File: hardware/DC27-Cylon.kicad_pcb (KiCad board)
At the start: 2 copper layers, 79 x 102 mm, 78 parts, among them J1 CONN_04LOCK, J2 CONN_05LOCK, U1 STM32F030K6Tx, U2 AZ1117-3.3, U3 74HC595D_118, U4 74HC595D_118, U5 74HC595D_118, Y1 16MHz

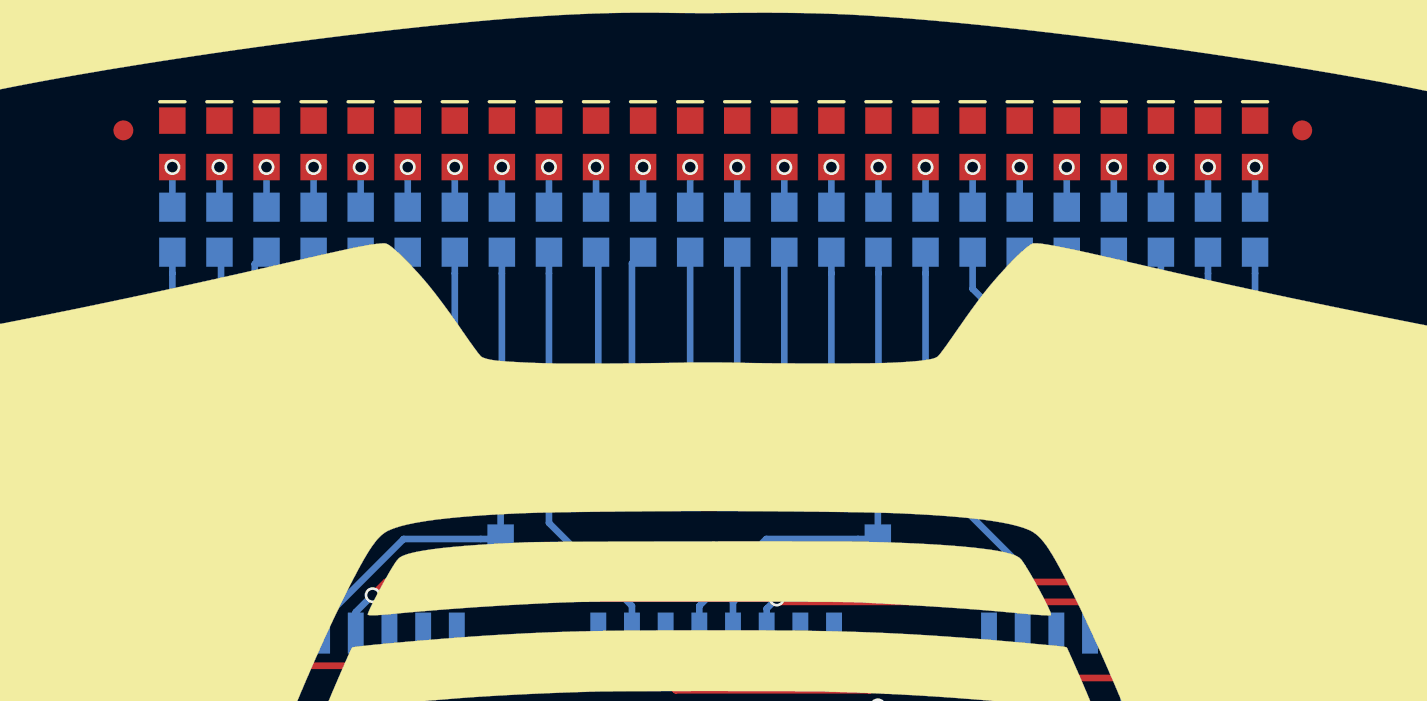
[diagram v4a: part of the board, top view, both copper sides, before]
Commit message: Remove via in pad
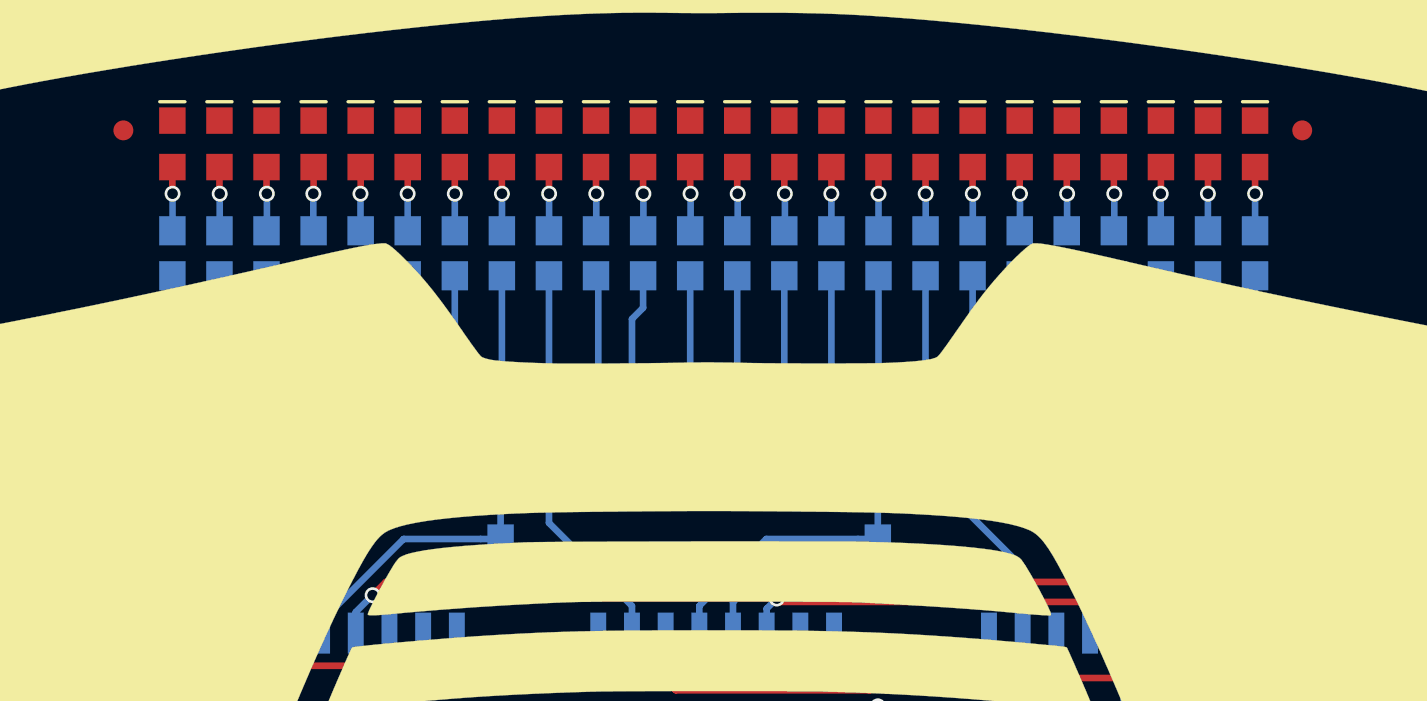
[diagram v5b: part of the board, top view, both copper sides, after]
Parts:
- removed the G*** at (59.4, 73.4) (x2)
- added G*** (x2): LOGO, LOGO, F.Cu at (59.4, 73.4)
- moved R1 0.89 mm to (80.0, 80.3)
- moved R10 0.89 mm to (64.0, 80.3)
- moved R11 0.89 mm to (62.3, 80.3)
- moved R12 0.89 mm to (60.5, 80.3)
- moved R13 0.89 mm to (58.7, 80.3)
- moved R14 0.89 mm to (56.9, 80.3)
- moved R15 0.89 mm to (55.2, 80.3)
- moved R16 0.89 mm to (53.4, 80.3)
- moved R17 0.89 mm to (51.6, 80.3)
- moved R18 0.89 mm to (49.8, 80.3)
- moved R19 0.89 mm to (48.1, 80.3)
- moved R2 0.89 mm to (78.2, 80.3)
- moved R20 0.89 mm to (46.3, 80.3)
- moved R21 0.89 mm to (44.5, 80.3)
- moved R22 0.89 mm to (42.7, 80.3)
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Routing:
- net Net-(D11-PadA): track 1.51 -> 2.42 mm
- net Net-(D12-PadA): track 1.51 -> 2.42 mm
- net Net-(D4-PadA): track 1.51 -> 2.42 mm
- net Net-(D13-PadA): track 1.51 -> 2.41 mm
- net Net-(D5-PadA): track 1.51 -> 2.41 mm
- net Net-(D22-PadA): track 1.51 -> 2.41 mm
- net Net-(D14-PadA): track 1.51 -> 2.41 mm
- net Net-(D6-PadA): track 1.51 -> 2.41 mm
- net Net-(D23-PadA): track 1.51 -> 2.41 mm
- net Net-(D21-PadA): track 1.51 -> 2.41 mm
- net Net-(D15-PadA): track 1.51 -> 2.41 mm
- net Net-(D7-PadA): track 1.51 -> 2.41 mm
- net Net-(D24-PadA): track 1.51 -> 2.41 mm
- net Net-(D20-PadA): track 1.51 -> 2.41 mm
- net Net-(D3-PadA): track 1.51 -> 2.41 mm
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
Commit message: Add SAO to head
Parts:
- removed the G*** at (59.4, 73.4) (x2)
- added G*** (x2): LOGO, LOGO, F.Cu at (59.4, 73.4)
- added SAO1: SAO, Sparkfun_Connectors:2X3, F.Cu at (41.5, 54.3)
- renumbered D24 to D1, D15 to D1, D14 to D1, D13 to D1, D12 to D1, D11 to D1, D10 to D1, D9 to D1, D8 to D1, D7 to D1, D6 to D1, D23 to D1, D5 to D1, D4 to D1, D3 to D1, D2 to D1, D22 to D1, D21 to D1, D20 to D1, D19 to D1, D18 to D1, D17 to D1, D16 to D1, R24 to R1, R15 to R1, R14 to R1, R13 to R1, R12 to R1, R11 to R1, R10 to R1, R9 to R1, R8 to R1, R7 to R1, R6 to R1, R23 to R1, R5 to R1, R4 to R1, R3 to R1, R2 to R1, R22 to R1, R21 to R1, R20 to R1, R19 to R1, R18 to R1, R17 to R1, R16 to R1
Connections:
- D1 pad A: Net-(D24-PadA) -> Net-(D1-PadA)
- D1 pad A: Net-(D15-PadA) -> Net-(D1-PadA)
- D1 pad A: Net-(D14-PadA) -> Net-(D1-PadA)
- D1 pad A: Net-(D13-PadA) -> Net-(D1-PadA)
- D1 pad A: Net-(D12-PadA) -> Net-(D1-PadA)
- D1 pad A: Net-(D11-PadA) -> Net-(D1-PadA)
- D1 pad A: Net-(D10-PadA) -> Net-(D1-PadA)
- D1 pad A: Net-(D9-PadA) -> Net-(D1-PadA)
- D1 pad A: Net-(D8-PadA) -> Net-(D1-PadA)
- D1 pad A: Net-(D7-PadA) -> Net-(D1-PadA)
- D1 pad A: Net-(D6-PadA) -> Net-(D1-PadA)
- D1 pad A: Net-(D23-PadA) -> Net-(D1-PadA)
- D1 pad A: Net-(D5-PadA) -> Net-(D1-PadA)
- D1 pad A: Net-(D4-PadA) -> Net-(D1-PadA)
- D1 pad A: Net-(D3-PadA) -> Net-(D1-PadA)
- D1 pad A: Net-(D2-PadA) -> Net-(D1-PadA)
- D1 pad A: Net-(D22-PadA) -> Net-(D1-PadA)
- D1 pad A: Net-(D21-PadA) -> Net-(D1-PadA)
- D1 pad A: Net-(D20-PadA) -> Net-(D1-PadA)
- D1 pad A: Net-(D19-PadA) -> Net-(D1-PadA)
- D1 pad A: Net-(D18-PadA) -> Net-(D1-PadA)
- D1 pad A: Net-(D17-PadA) -> Net-(D1-PadA)
- D1 pad A: Net-(D16-PadA) -> Net-(D1-PadA)
- R1 pad 1: /LED23 -> /LED0
- R1 pad 2: Net-(D24-PadA) -> Net-(D1-PadA)
- R1 pad 1: /LED14 -> /LED0
- R1 pad 2: Net-(D15-PadA) -> Net-(D1-PadA)
- R1 pad 1: /LED13 -> /LED0
- R1 pad 2: Net-(D14-PadA) -> Net-(D1-PadA)
- R1 pad 1: /LED12 -> /LED0
- R1 pad 2: Net-(D13-PadA) -> Net-(D1-PadA)
- R1 pad 1: /LED11 -> /LED0
- R1 pad 2: Net-(D12-PadA) -> Net-(D1-PadA)
- R1 pad 1: /LED10 -> /LED0
- R1 pad 2: Net-(D11-PadA) -> Net-(D1-PadA)
- R1 pad 1: /LED9 -> /LED0
- R1 pad 2: Net-(D10-PadA) -> Net-(D1-PadA)
- R1 pad 1: /LED8 -> /LED0
- R1 pad 2: Net-(D9-PadA) -> Net-(D1-PadA)
- R1 pad 1: /LED7 -> /LED0
- R1 pad 2: Net-(D8-PadA) -> Net-(D1-PadA)
- R1 pad 1: /LED6 -> /LED0
- R1 pad 2: Net-(D7-PadA) -> Net-(D1-PadA)
- R1 pad 1: /LED5 -> /LED0
- R1 pad 2: Net-(D6-PadA) -> Net-(D1-PadA)
- R1 pad 1: /LED22 -> /LED0
- R1 pad 2: Net-(D23-PadA) -> Net-(D1-PadA)
- R1 pad 1: /LED4 -> /LED0
- R1 pad 2: Net-(D5-PadA) -> Net-(D1-PadA)
- R1 pad 1: /LED3 -> /LED0
- R1 pad 2: Net-(D4-PadA) -> Net-(D1-PadA)
- R1 pad 1: /LED2 -> /LED0
- R1 pad 2: Net-(D3-PadA) -> Net-(D1-PadA)
- R1 pad 1: /LED1 -> /LED0
- R1 pad 2: Net-(D2-PadA) -> Net-(D1-PadA)
- R1 pad 1: /LED21 -> /LED0
- R1 pad 2: Net-(D22-PadA) -> Net-(D1-PadA)
- R1 pad 1: /LED20 -> /LED0
- R1 pad 2: Net-(D21-PadA) -> Net-(D1-PadA)
- R1 pad 1: /LED19 -> /LED0
- R1 pad 2: Net-(D20-PadA) -> Net-(D1-PadA)
- R1 pad 1: /LED18 -> /LED0
- R1 pad 2: Net-(D19-PadA) -> Net-(D1-PadA)
- R1 pad 1: /LED17 -> /LED0
- R1 pad 2: Net-(D18-PadA) -> Net-(D1-PadA)
- R1 pad 1: /LED16 -> /LED0
- R1 pad 2: Net-(D17-PadA) -> Net-(D1-PadA)
- R1 pad 1: /LED15 -> /LED0
- R1 pad 2: Net-(D16-PadA) -> Net-(D1-PadA)
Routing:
- net Net-(D1-PadA): track 2.40 -> 57.8 mm, vias 1 -> 24
- net Net-(D11-PadA): track 2.42 -> 0.00 mm, vias 1 -> 0
- net Net-(D12-PadA): track 2.42 -> 0.00 mm, vias 1 -> 0
- net Net-(D4-PadA): track 2.42 -> 0.00 mm, vias 1 -> 0
- net Net-(D13-PadA): track 2.41 -> 0.00 mm, vias 1 -> 0
- net Net-(D5-PadA): track 2.41 -> 0.00 mm, vias 1 -> 0
- net Net-(D22-PadA): track 2.41 -> 0.00 mm, vias 1 -> 0
- net Net-(D14-PadA): track 2.41 -> 0.00 mm, vias 1 -> 0
- net Net-(D6-PadA): track 2.41 -> 0.00 mm, vias 1 -> 0
- net Net-(D23-PadA): track 2.41 -> 0.00 mm, vias 1 -> 0
- net Net-(D21-PadA): track 2.41 -> 0.00 mm, vias 1 -> 0
- net Net-(D15-PadA): track 2.41 -> 0.00 mm, vias 1 -> 0
- net Net-(D7-PadA): track 2.41 -> 0.00 mm, vias 1 -> 0
- net Net-(D24-PadA): track 2.41 -> 0.00 mm, vias 1 -> 0
- net Net-(D20-PadA): track 2.41 -> 0.00 mm, vias 1 -> 0
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
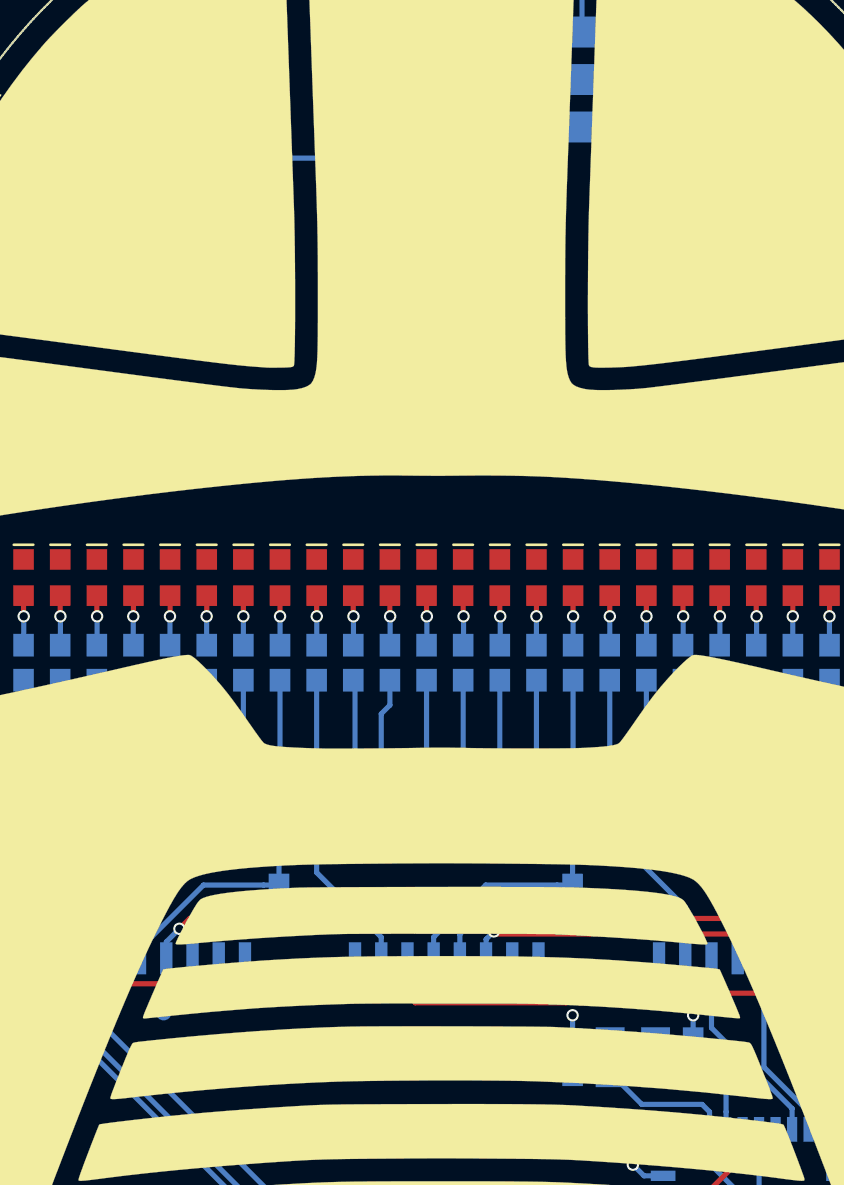
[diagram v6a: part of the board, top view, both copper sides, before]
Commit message: Move some small traces a little, update BOMs
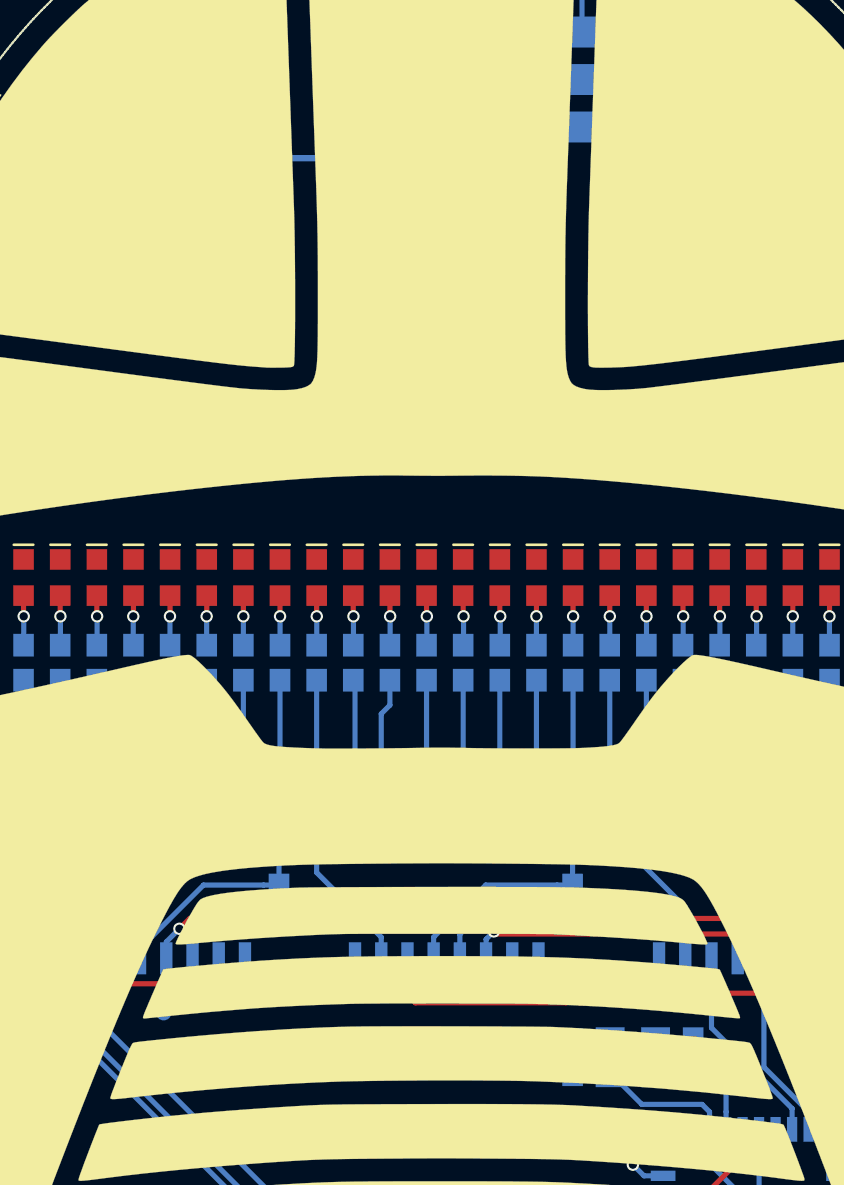
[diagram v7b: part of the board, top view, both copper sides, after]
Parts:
- removed the G*** at (59.4, 73.4) (x2)
- added G*** (x2): LOGO, LOGO, F.Cu at (59.4, 73.4)
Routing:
- net GND: track 54.1 -> 61.6 mm
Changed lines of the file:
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@@
     (thickness 1.6)
     (drawings 1827)
-    (tracks 411)
+    (tracks 414)
     (zones 0)
     (modules 79)
@@
   (page A4)
   (layers
-    (0 F.Cu signal)
+    (0 F.Cu signal hide)
     (31 B.Cu signal)
-    (32 B.Adhes user)
-    (33 F.Adhes user)
-    (34 B.Paste user)
-    (35 F.Paste user)
-    (36 B.SilkS user)
-    (37 F.SilkS user)
-    (38 B.Mask user)
-    (39 F.Mask user)
+    (32 B.Adhes user hide)
+    (33 F.Adhes user hide)
+    (34 B.Paste user hide)
+    (35 F.Paste user hide)
+    (36 B.SilkS user hide)
+    (37 F.SilkS user hide)
+    (38 B.Mask user hide)
+    (39 F.Mask user hide)
     (40 Dwgs.User user)
     (41 Cmts.User user)
@@
   (gr_line (start 59.86389 116.45791) (end 60.078076 116.45391) (layer Edge.Cuts) (width 0.1))
   (gr_line (start 60.078076 116.45391) (end 60.078842 116.44949) (layer Edge.Cuts) (width 0.1))
-  (segment (start 65.994 54.37) (end 64.484 55.88) (width 0.25) (layer B.Cu) (net 1))
+  (segment (start 65.994 54.37) (end 64.484 55.88) (width 0.3048) (layer B.Cu) (net 1))
   (segment (start 66.244 54.37) (end 65.994 54.37) (width 0.25) (layer B.Cu) (net 1))
-  (segment (start 45.446 58.801) (end 44.196 58.801) (width 0.25) (layer B.Cu) (net 1))
-  (segment (start 48.367 55.88) (end 45.446 58.801) (width 0.25) (layer B.Cu) (net 1))
-  (segment (start 64.484 55.88) (end 48.367 55.88) (width 0.25) (layer B.Cu) (net 1))
+  (segment (start 45.446 58.801) (end 44.196 58.801) (width 0.3048) (layer B.Cu) (net 1))
+  (segment (start 48.367 55.88) (end 45.446 58.801) (width 0.3048) (layer B.Cu) (net 1))
+  (segment (start 64.484 55.88) (end 48.367 55.88) (width 0.3048) (layer B.Cu) (net 1))
   (segment (start 68.98764 54.37) (end 69.00164 54.356) (width 0.25) (layer B.Cu) (net 1))
   (segment (start 66.244 54.37) (end 68.98764 54.37) (width 0.25) (layer B.Cu) (net 1))
@@
   (segment (start 59.055 94.648) (end 59.055 93.623) (width 0.25) (layer B.Cu) (net 2))
   (segment (start 61.57836 91.09964) (end 65.03689 91.09964) (width 0.25) (layer B.Cu) (net 2))
-  (via (at 71.628 97.409) (size 0.6) (drill 0.4) (layers F.Cu B.Cu) (net 2))
-  (segment (start 71.628 98.54164) (end 71.628 97.409) (width 0.25) (layer B.Cu) (net 2))
-  (via (at 65.786 97.409) (size 0.6) (drill 0.4) (layers F.Cu B.Cu) (net 2))
-  (segment (start 65.786 98.59264) (end 65.786 97.409) (width 0.25) (layer B.Cu) (net 2))
   (via (at 68.707 104.648) (size 0.6) (drill 0.4) (layers F.Cu B.Cu) (net 2))
   (segment (start 70.172 104.388) (end 68.967 104.388) (width 0.25) (layer B.Cu) (net 2))
@@
   (segment (start 69.247 105.188) (end 68.707 104.648) (width 0.25) (layer B.Cu) (net 2))
   (segment (start 70.172 105.188) (end 69.247 105.188) (width 0.25) (layer B.Cu) (net 2))
+  (via (at 64.516 98.552) (size 0.6) (drill 0.4) (layers F.Cu B.Cu) (net 2))
+  (segment (start 65.786 98.59264) (end 64.55664 98.59264) (width 0.25) (layer B.Cu) (net 2))
+  (segment (start 64.55664 98.59264) (end 64.516 98.552) (width 0.25) (layer B.Cu) (net 2))
+  (segment (start 64.516 98.552) (end 71.755 98.552) (width 0.25) (layer F.Cu) (net 2))
+  (via (at 72.644 99.314) (size 0.6) (drill 0.4) (layers F.Cu B.Cu) (net 2))
+  (segment (start 71.628 98.54164) (end 71.87164 98.54164) (width 0.25) (layer B.Cu) (net 2))
+  (segment (start 71.87164 98.54164) (end 72.644 99.314) (width 0.25) (layer B.Cu) (net 2))
   (segment (start 67.607 98.591) (end 67.607 100.291) (width 0.25) (layer B.Cu) (net 3))
   (segment (start 67.60536 100.28936) (end 67.607 100.291) (width 0.25) (layer B.Cu) (net 3))

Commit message: add some small silkscreen
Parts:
- removed the G*** at (59.4, 73.4) (x2)
- added G*** (x2): LOGO, LOGO, F.Cu at (59.4, 73.4)
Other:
- board text added: "@TBazooka"
- board text added: "github.com/TeamBazooka/DC27/"
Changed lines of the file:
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@@
   (general
     (thickness 1.6)
-    (drawings 1827)
+    (drawings 1829)
     (tracks 414)
     (zones 0)
@@
   (page A4)
   (layers
-    (0 F.Cu signal hide)
+    (0 F.Cu signal)
     (31 B.Cu signal)
-    (32 B.Adhes user hide)
-    (33 F.Adhes user hide)
-    (34 B.Paste user hide)
-    (35 F.Paste user hide)
-    (36 B.SilkS user hide)
-    (37 F.SilkS user hide)
-    (38 B.Mask user hide)
-    (39 F.Mask user hide)
+    (32 B.Adhes user)
+    (33 F.Adhes user)
+    (34 B.Paste user)
+    (35 F.Paste user)
+    (36 B.SilkS user)
+    (37 F.SilkS user)
+    (38 B.Mask user)
+    (39 F.Mask user)
     (40 Dwgs.User user)
     (41 Cmts.User user)
@@
     (visible_elements FFFFFF7F)
     (pcbplotparams
-      (layerselection 0x010fc_ffffffff)
+      (layerselection 0x310fc_ffffffff)
       (usegerberextensions false)
       (usegerberattributes false)
@@
     )
   )
+  (gr_text github.com/TeamBazooka/DC27/ (at 59.944 45.339) (layer B.SilkS)
+    (effects (font (size 1 1) (thickness 0.15)) (justify mirror))
+  )
+  (gr_text @TBazooka (at 59.436 41.91) (layer B.SilkS)
+    (effects (font (size 1 1) (thickness 0.15)) (justify mirror))
+  )
   (gr_circle (center 68.834 89.154) (end 68.58 89.154) (layer B.SilkS) (width 0.15))
